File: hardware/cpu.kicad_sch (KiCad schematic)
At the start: 4 parts, among them U3 Pico, U4 74HC595

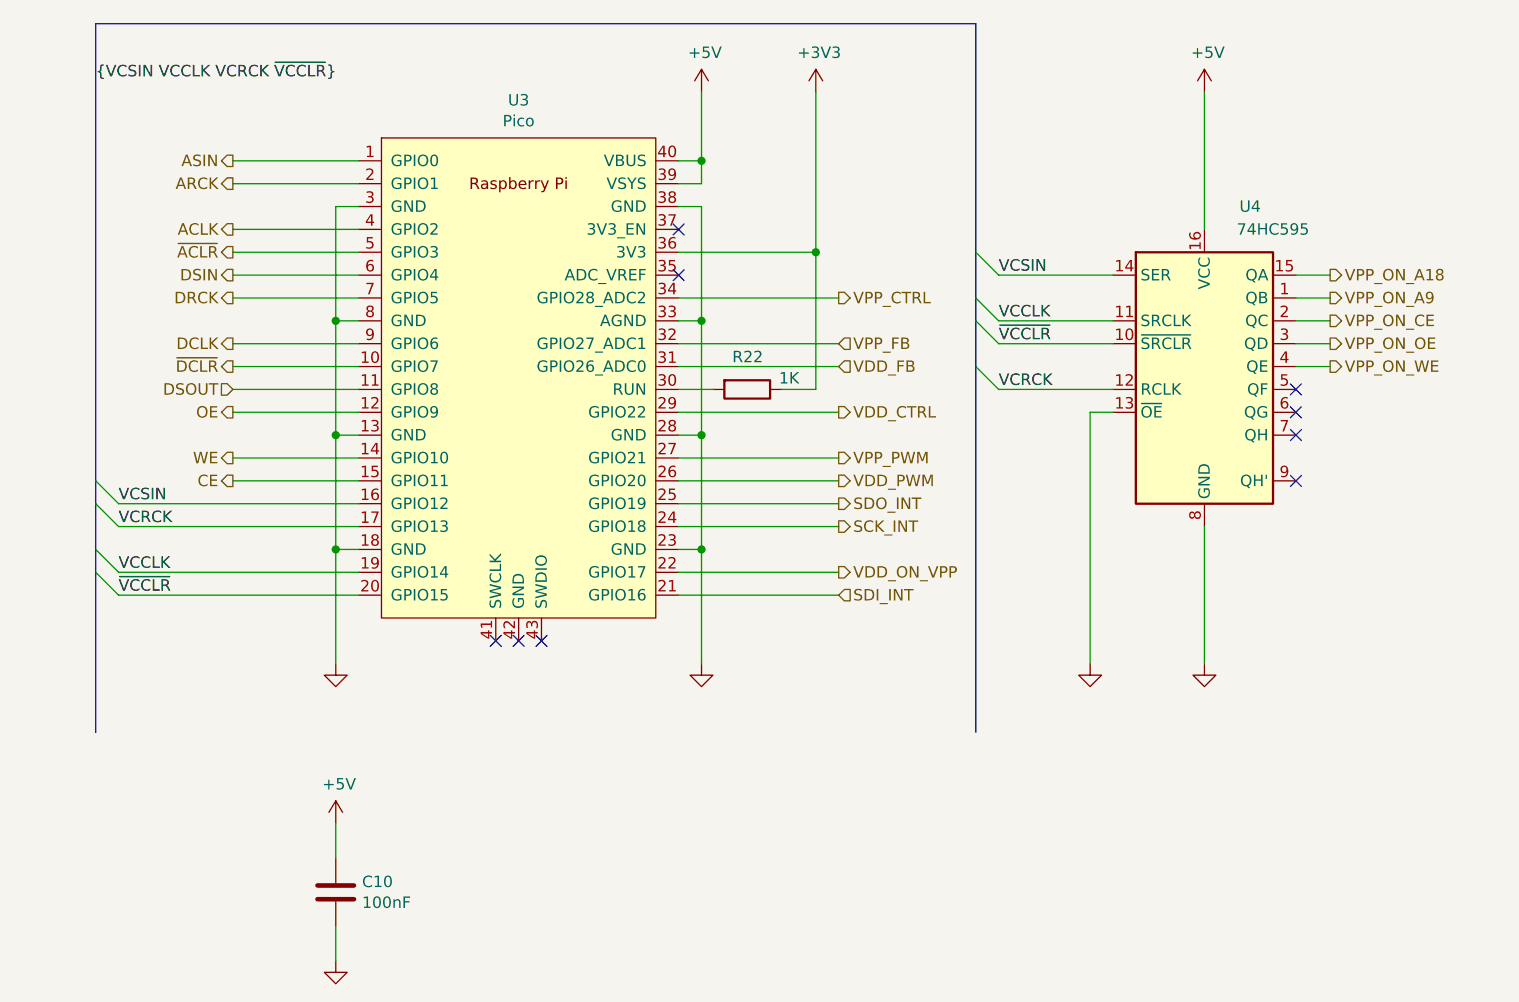
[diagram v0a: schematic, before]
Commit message: Rev.E. Updated hardware design.
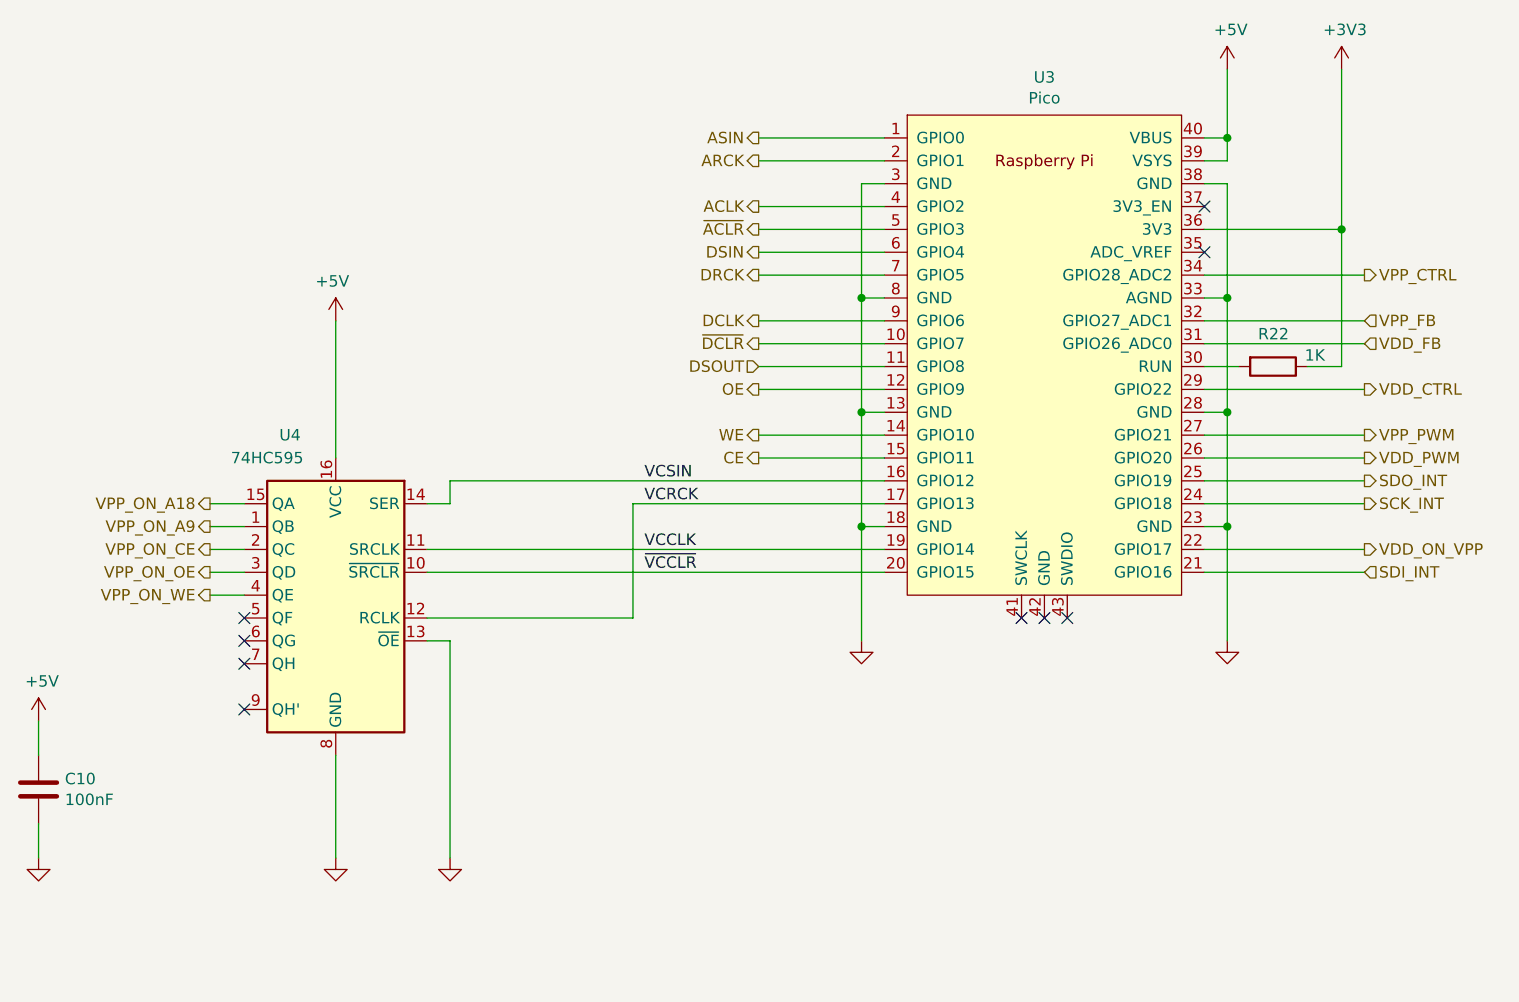
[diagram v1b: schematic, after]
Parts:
- U3: footprint (none) -> MCU_RaspberryPi_and_Boards:RPi_Pico_SMD_TH
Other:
- moved on the sheet: C10, R22, U3, U4
